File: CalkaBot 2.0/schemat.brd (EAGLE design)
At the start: 94.4 x 101.8 mm, 55 parts, among them IC1 TB6612FNG, IC2 LM339D, IC3 7806DT, Q1 16MHz, X1 MINI-USB-32005-301

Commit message: niezapisane rzeczt
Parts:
- added U$2, U$4, U$5: (no value), untitled:GND@1
- added U$3: (no value), untitled:GND
- moved X1 80.3 mm to (8.10, 81.7)
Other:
- board text added: "A1"
- board text added: "A2"
- board text added: "A4"
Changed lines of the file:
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@@
 <grid distance="0.1" unitdist="mm" unit="mm" style="lines" multiple="1" display="yes" altdistance="0.01" altunitdist="mm" altunit="mm"/>
 <layers>
-<layer number="1" name="Top" color="4" fill="1" visible="yes" active="yes"/>
+<layer number="1" name="Top" color="4" fill="1" visible="no" active="yes"/>
 <layer number="16" name="Bottom" color="1" fill="1" visible="yes" active="yes"/>
 <layer number="17" name="Pads" color="2" fill="1" visible="yes" active="yes"/>
 <layer number="18" name="Vias" color="2" fill="1" visible="yes" active="yes"/>
-<layer number="19" name="Unrouted" color="6" fill="1" visible="yes" active="yes"/>
-<layer number="20" name="Dimension" color="24" fill="1" visible="yes" active="yes"/>
-<layer number="21" name="tPlace" color="7" fill="1" visible="yes" active="yes"/>
-<layer number="22" name="bPlace" color="7" fill="1" visible="yes" active="yes"/>
-<layer number="23" name="tOrigins" color="15" fill="1" visible="yes" active="yes"/>
-<layer number="24" name="bOrigins" color="15" fill="1" visible="yes" active="yes"/>
-<layer number="25" name="tNames" color="7" fill="1" visible="yes" active="yes"/>
-<layer number="26" name="bNames" color="7" fill="1" visible="yes" active="yes"/>
-<layer number="27" name="tValues" color="7" fill="1" visible="yes" active="yes"/>
-<layer number="28" name="bValues" color="7" fill="1" visible="yes" active="yes"/>
+<layer number="19" name="Unrouted" color="6" fill="1" visible="no" active="yes"/>
+<layer number="20" name="Dimension" color="24" fill="1" visible="no" active="yes"/>
+<layer number="21" name="tPlace" color="7" fill="1" visible="no" active="yes"/>
+<layer number="22" name="bPlace" color="7" fill="1" visible="no" active="yes"/>
+<layer number="23" name="tOrigins" color="15" fill="1" visible="no" active="yes"/>
+<layer number="24" name="bOrigins" color="15" fill="1" visible="no" active="yes"/>
+<layer number="25" name="tNames" color="7" fill="1" visible="no" active="yes"/>
+<layer number="26" name="bNames" color="7" fill="1" visible="no" active="yes"/>
+<layer number="27" name="tValues" color="7" fill="1" visible="no" active="yes"/>
+<layer number="28" name="bValues" color="7" fill="1" visible="no" active="yes"/>
 <layer number="29" name="tStop" color="7" fill="3" visible="no" active="yes"/>
 <layer number="30" name="bStop" color="7" fill="6" visible="no" active="yes"/>
@@
 <layer number="37" name="tTest" color="7" fill="1" visible="no" active="yes"/>
 <layer number="38" name="bTest" color="7" fill="1" visible="no" active="yes"/>
-<layer number="39" name="tKeepout" color="4" fill="11" visible="yes" active="yes"/>
-<layer number="40" name="bKeepout" color="1" fill="11" visible="yes" active="yes"/>
-<layer number="41" name="tRestrict" color="4" fill="10" visible="yes" active="yes"/>
-<layer number="42" name="bRestrict" color="1" fill="10" visible="yes" active="yes"/>
+<layer number="39" name="tKeepout" color="4" fill="11" visible="no" active="yes"/>
+<layer number="40" name="bKeepout" color="1" fill="11" visible="no" active="yes"/>
+<layer number="41" name="tRestrict" color="4" fill="10" visible="no" active="yes"/>
+<layer number="42" name="bRestrict" color="1" fill="10" visible="no" active="yes"/>
 <layer number="43" name="vRestrict" color="2" fill="10" visible="no" active="yes"/>
-<layer number="44" name="Drills" color="7" fill="1" visible="yes" active="yes"/>
-<layer number="45" name="Holes" color="7" fill="1" visible="yes" active="yes"/>
+<layer number="44" name="Drills" color="7" fill="1" visible="no" active="yes"/>
+<layer number="45" name="Holes" color="7" fill="1" visible="no" active="yes"/>
 <layer number="46" name="Milling" color="3" fill="1" visible="no" active="yes"/>
 <layer number="47" name="Measures" color="7" fill="1" visible="no" active="yes"/>
@@
 <layer number="49" name="Reference" color="7" fill="1" visible="no" active="yes"/>
 <layer number="50" name="dxf" color="7" fill="1" visible="no" active="no"/>
-<layer number="51" name="tDocu" color="7" fill="1" visible="yes" active="yes"/>
-<layer number="52" name="bDocu" color="7" fill="1" visible="yes" active="yes"/>
+<layer number="51" name="tDocu" color="7" fill="1" visible="no" active="yes"/>
+<layer number="52" name="bDocu" color="7" fill="1" visible="no" active="yes"/>
 <layer number="53" name="tGND_GNDA" color="7" fill="9" visible="no" active="no"/>
 <layer number="54" name="bGND_GNDA" color="1" fill="9" visible="no" active="no"/>
@@
 <text x="17" y="8.7" size="1.016" layer="16" font="vector" ratio="25" rot="MR0" align="center">S4</text>
 <text x="83.2" y="8.6" size="1.016" layer="16" font="vector" ratio="25" rot="MR0" align="center">A3</text>
+<text x="14.7" y="66.2" size="1.016" layer="16" font="vector" ratio="25" rot="MR0" align="center">A2</text>
+<text x="14.7" y="8.7" size="1.016" layer="16" font="vector" ratio="25" rot="MR0" align="center">A4</text>
+<text x="83.1" y="66.2" size="1.016" layer="16" font="vector" ratio="25" rot="MR0" align="center">A1</text>
 </plain>
 <attributes>
@@
 <attribute name="OC_NEWARK" value="36M3542" x="24.2" y="3.8" size="1.778" layer="28" rot="MR0" display="off"/>
 </element>
-<element name="X1" library="con-cypressindustries" library_urn="urn:adsk.eagle:library:138" package="32005-301" package3d_urn="urn:adsk.eagle:package:6446/1" value="MINI-USB-32005-301" x="88.1" y="75.2" rot="MR270">
-<attribute name="MF" value="" x="88.1" y="75.2" size="1.778" layer="28" rot="MR270" display="off"/>
-<attribute name="MPN" value="" x="88.1" y="75.2" size="1.778" layer="28" rot="MR270" display="off"/>
-<attribute name="OC_FARNELL" value="unknown" x="88.1" y="75.2" size="1.778" layer="28" rot="MR270" display="off"/>
-<attribute name="OC_NEWARK" value="unknown" x="88.1" y="75.2" size="1.778" layer="28" rot="MR270" display="off"/>
+<element name="X1" library="con-cypressindustries" library_urn="urn:adsk.eagle:library:138" package="32005-301" package3d_urn="urn:adsk.eagle:package:6446/1" value="MINI-USB-32005-301" x="8.1" y="81.7" rot="MR270">
+<attribute name="MF" value="" x="8.1" y="81.7" size="1.778" layer="28" rot="MR270" display="off"/>
+<attribute name="MPN" value="" x="8.1" y="81.7" size="1.778" layer="28" rot="MR270" display="off"/>
+<attribute name="OC_FARNELL" value="unknown" x="8.1" y="81.7" size="1.778" layer="28" rot="MR270" display="off"/>
+<attribute name="OC_NEWARK" value="unknown" x="8.1" y="81.7" size="1.778" layer="28" rot="MR270" display="off"/>
 </element>
 <element name="R6" library="rcl" library_urn="urn:adsk.eagle:library:334" package="R0805" package3d_urn="urn:adsk.eagle:package:23553/2" value="10k" x="24.3" y="21.8" rot="R270">
@@
 <element name="JP2" library="pinhead" library_urn="urn:adsk.eagle:library:325" package="1X05" package3d_urn="urn:adsk.eagle:package:22469/2" value="" x="27.5" y="39.9" rot="MR90"/>
 <element name="JP3" library="pinhead" library_urn="urn:adsk.eagle:library:325" package="1X05" package3d_urn="urn:adsk.eagle:package:22469/2" value="" x="20.9" y="39.9" rot="MR90"/>
+<element name="U$2" library="untitled" package="GND@1" value="" x="85.5" y="8.5"/>
+<element name="U$4" library="untitled" package="GND@1" value="" x="85.4" y="66"/>
+<element name="U$5" library="untitled" package="GND@1" value="" x="12.4" y="66"/>
+<element name="U$3" library="untitled" package="GND" value="" x="-39.5" y="-20.7">
+<attribute name="UZ" value="gnd" x="-39.5" y="-20.7" size="1.778" layer="27" display="off"/>
+</element>
 </elements>
 <signals>
@@
 <wire x1="85.4" y1="59.33555" x2="85.4" y2="67.7" width="0.4" layer="1"/>
 <wire x1="84.2" y1="56" x2="85.48389375" y2="57.28389375" width="0.4" layer="1"/>
-<wire x1="85.48389375" y1="57.28389375" x2="85.48389375" y2="58.1" width="0.4" layer="1"/>
-<wire x1="85.48389375" y1="58.1" x2="85.48389375" y2="59.25165625" width="0.4" layer="1"/>
-<wire x1="87.3" y1="72.2" x2="86.5" y2="72.2" width="0" layer="19" extent="16-16"/>
-<wire x1="85.4" y1="67.7" x2="86.5" y2="72.2" width="0" layer="19" extent="16-16"/>
+<wire x1="85.48389375" y1="57.28389375" x2="85.48389375" y2="59.25165625" width="0.4" layer="1"/>
+<wire x1="7.3" y1="78.7" x2="6.5" y2="78.7" width="0" layer="19" extent="16-16"/>
+<wire x1="85.4" y1="67.7" x2="6.5" y2="78.7" width="0" layer="19" extent="16-16"/>
 <wire x1="20.9" y1="34.82" x2="20.9488" y2="32.3606" width="0" layer="19" extent="1-1"/>
 <wire x1="27.4512" y1="25.4606" x2="28.4" y2="30.1" width="0" layer="19" extent="1-1"/>
 <wire x1="27.4512" y1="18.5606" x2="20.9488" y2="18.5606" width="0" layer="19" extent="1-1"/>
-<wire x1="85.48389375" y1="58.1" x2="85.48389375" y2="58.1" width="0.4" layer="1"/>
 </signal>
 <signal name="RST">
@@
 <contactref element="JP3" pad="5"/>
 <wire x1="20.9" y1="44.98" x2="27.5" y2="44.98" width="0.4" layer="16"/>
-<wire x1="46.684465625" y1="33.78309375" x2="89.7" y2="72.2" width="0" layer="19" extent="1-16"/>
+<wire x1="46.684465625" y1="33.78309375" x2="9.7" y2="78.7" width="0" layer="19" extent="1-16"/>
 <wire x1="27.5" y1="44.98" x2="29.23005" y2="44.98" width="0" layer="19" extent="16-16"/>
 </signal>
@@
 <wire x1="20.9" y1="39.9" x2="27.5" y2="39.9" width="0.4" layer="16"/>
 <wire x1="27.5" y1="39.9" x2="27.6" y2="39.8" width="0.4" layer="16"/>
-<wire x1="33.3422875" y1="38.389946875" x2="88.1" y2="72.2" width="0" layer="19" extent="16-16"/>
+<wire x1="33.3422875" y1="38.389946875" x2="8.1" y2="78.7" width="0" layer="19" extent="16-16"/>
 </signal>
 <signal name="N$20">
@@
 <wire x1="31.26" y1="42.44" x2="27.5" y2="42.44" width="0.4" layer="16"/>
 <wire x1="27.5" y1="42.44" x2="20.9" y2="42.44" width="0.4" layer="16"/>
-<wire x1="35.4" y1="38.3" x2="88.9" y2="72.2" width="0" layer="19" extent="1-16"/>
+<wire x1="35.4" y1="38.3" x2="8.9" y2="78.7" width="0" layer="19" extent="1-16"/>
 </signal>
 <signal name="N$2">

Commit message: dodalem dipy
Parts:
- removed BUT1, BUT2, BUT3: (no value), switch-omron:B3F-10XX
- removed JP3: (no value), pinhead:1X05
- removed X1: MINI-USB-32005-301, con-cypressindustries:32005-301
- added SW2: (no value), special:EDG-03
- moved R2 8.16 mm to (25.3, 23.0), turned to 0 degrees
- moved R6 3.83 mm to (25.3, 25.5), turned to 0 degrees
- moved C10 2.94 mm to (34.8, 30.6)
- moved R9 1.17 mm to (25.3, 28.1), turned to 0 degrees
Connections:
- removed net N$20: JP2.4, JP3.4, R26.1, X1.4
- new net N$11: JP2.4, R26.1
- net GND: now also SW2.4, SW2.5, SW2.6; no longer BUT1.1, BUT1.2, BUT2.1, BUT2.2, BUT3.1, BUT3.2, JP3.1, JP3.2, X1.1, X1.2
- net MISO: now also SW2.3; no longer BUT1.3, BUT1.4
- net MOSI: now also SW2.2; no longer BUT2.3, BUT2.4
- net N$12: no longer JP3.3, X1.3
- net SCK: now also SW2.1; no longer BUT3.3, BUT3.4
- net VBUS: no longer JP3.5, X1.5
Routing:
- net VCC: track 297.7 -> 339.1 mm, vias 5 -> 4
- net N$20: track 18.0 -> 0.00 mm, vias 1 -> 0
- net MISO: track 35.7 -> 26.3 mm
- net MOSI: track 33.1 -> 25.8 mm
- net N$12: track 15.0 -> 8.41 mm
- net SCK: track 29.0 -> 23.5 mm
- net VBUS: track 36.9 -> 32.0 mm
- net GND: track 446.3 -> 441.9 mm, vias 5 -> 6
- net UCAP: track 14.6 -> 11.4 mm
- net VM: track 80.7 -> 80.1 mm

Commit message: połączono wszystkie VCC i GND
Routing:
- net VCC: track 339.1 -> 454.4 mm, vias 4 -> 5
- net N$11: track 0.00 -> 12.2 mm
- net GND: track 441.9 -> 450.5 mm
- net PIN: track 26.4 -> 25.2 mm
- net MOSI: track 25.8 -> 24.9 mm
- net N$12: vias 1 -> 0

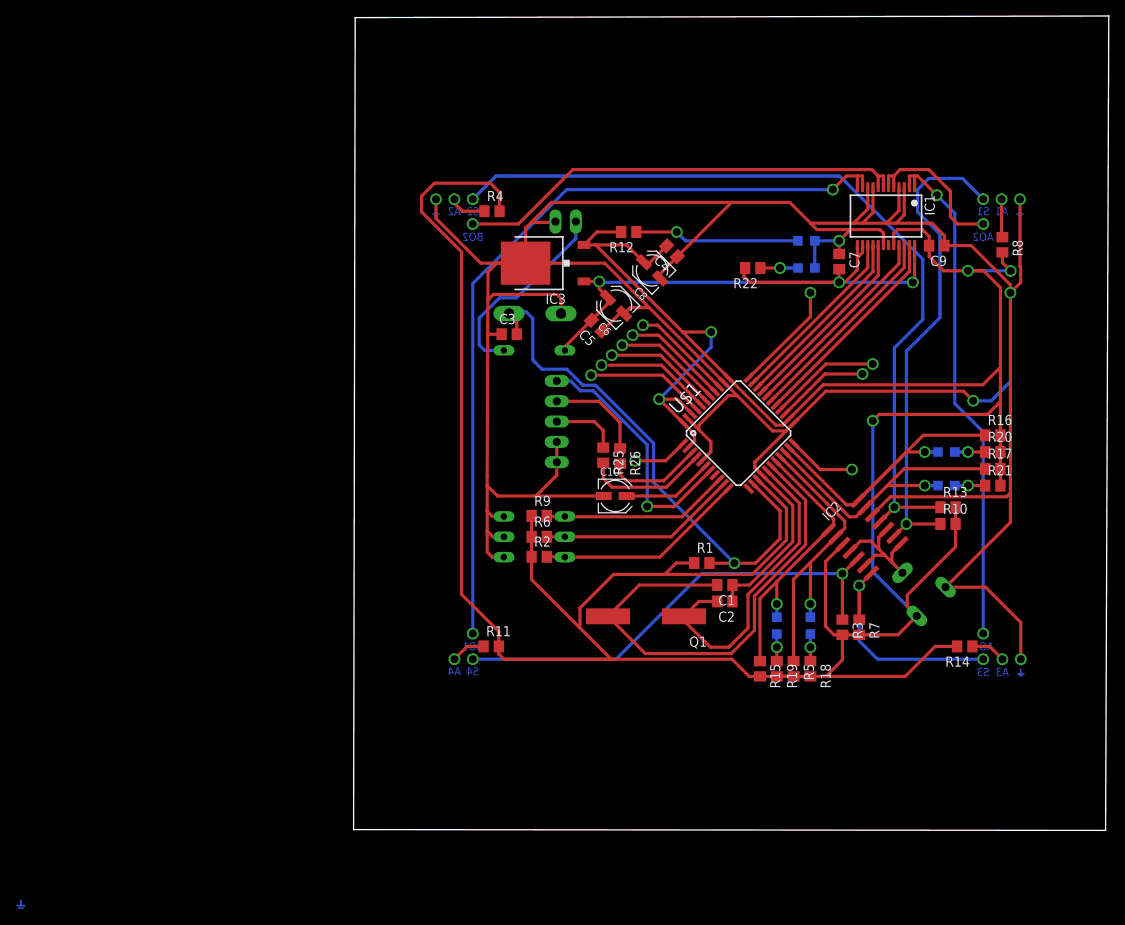
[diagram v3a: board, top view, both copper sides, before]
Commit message: dodano diode
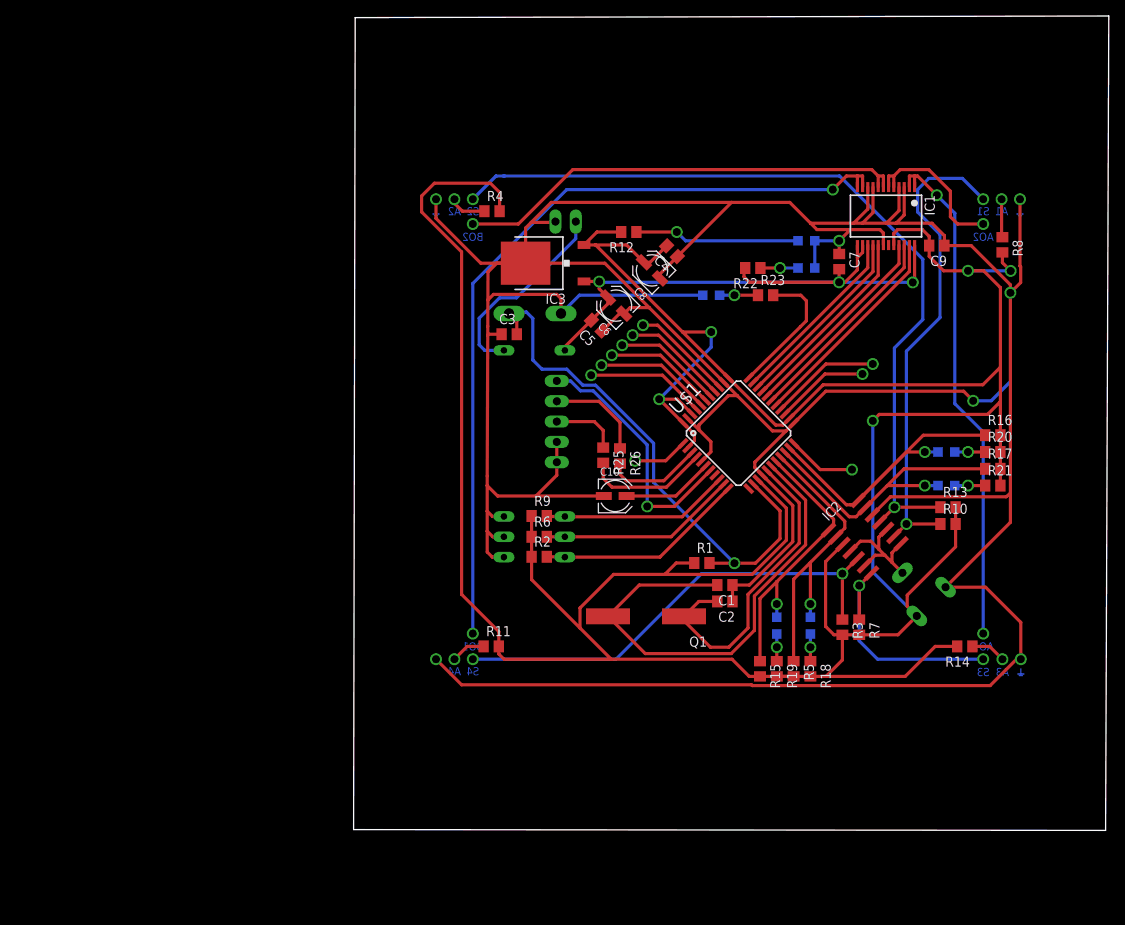
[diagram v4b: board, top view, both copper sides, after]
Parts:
- removed U$3: (no value), untitled:GND
- added LED7: (no value), led:CHIP-LED0805
- added R23: 220R, rcl:R0805
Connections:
- new net N$2: LED7.A, R23.1
- net GND: now also LED7.C
- net I/O10: now also R23.2
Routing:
- net GND: track 450.5 -> 545.0 mm, vias 6 -> 7
- net N$2: track 0.00 -> 4.80 mm, vias 0 -> 1
- net I/O10: track 13.8 -> 17.1 mm, vias 1 -> 0
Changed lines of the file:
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@@
 <text x="80.8" y="63" size="1.016" layer="16" font="vector" ratio="25" rot="MR0" align="center">AO2</text>
 <text x="80.8" y="11.8" size="1.016" layer="16" font="vector" ratio="25" rot="MR0" align="center">AO1</text>
-<wire x1="17" y1="85.1" x2="17.8" y2="85.9" width="0.4" layer="19"/>
 <text x="80.8" y="66.2" size="1.016" layer="16" font="vector" ratio="25" rot="MR0" align="center">S1</text>
 <text x="17" y="66.2" size="1.016" layer="16" font="vector" ratio="25" rot="MR0" align="center">S2</text>
@@
 <element name="U$4" library="untitled" package="GND@1" value="" x="85.4" y="66" smashed="yes"/>
 <element name="U$5" library="untitled" package="GND@1" value="" x="12.4" y="66" smashed="yes"/>
-<element name="U$3" library="untitled" package="GND" value="" x="-39.5" y="-20.7" smashed="yes">
-<attribute name="UZ" value="gnd" x="-39.5" y="-20.7" size="1.778" layer="27" display="off"/>
-</element>
 <element name="SW2" library="special" library_urn="urn:adsk.eagle:library:367" package="EDG-03" package3d_urn="urn:adsk.eagle:package:26663/2" value="" x="24.7" y="25.5" smashed="yes" rot="MR270">
 <attribute name="NAME" x="19.366" y="30.072" size="1.27" layer="26" ratio="10" rot="MR270"/>
 <attribute name="VALUE" x="31.304" y="30.072" size="1.27" layer="28" ratio="10" rot="MR270"/>
+</element>
+<element name="R23" library="rcl" library_urn="urn:adsk.eagle:library:334" package="R0805" package3d_urn="urn:adsk.eagle:package:23553/2" value="220R" x="53.6" y="55.7" smashed="yes">
+<attribute name="NAME" x="52.965" y="56.97" size="1.27" layer="25"/>
+<attribute name="SPICEPREFIX" value="R" x="53.6" y="55.7" size="1.778" layer="27" display="off"/>
+<attribute name="VALUE" x="52.965" y="53.16" size="1.27" layer="27"/>
+</element>
+<element name="LED7" library="led" library_urn="urn:adsk.eagle:library:259" package="CHIP-LED0805" package3d_urn="urn:adsk.eagle:package:15818/2" value="" x="46.8" y="55.7" smashed="yes" rot="MR270">
+<attribute name="NAME" x="48.07" y="56.97" size="1.27" layer="26" rot="MR0"/>
+<attribute name="VALUE" x="48.07" y="53.16" size="1.27" layer="28" rot="MR0"/>
 </element>
 </elements>
@@
 <contactref element="C9" pad="1"/>
 <contactref element="JP1" pad="1"/>
-<contactref element="LED5" pad="C"/>
 <wire x1="48.381521875" y1="44.813959375" x2="39.047740625" y2="54.147740625" width="0.4" layer="1"/>
 <wire x1="39.047740625" y1="54.147740625" x2="33.49548125" y2="59.7" width="0.4" layer="1"/>
@@
 <wire x1="40.407625" y1="57.792371875" x2="40.407625" y2="58.364121875" width="0.4" layer="1"/>
 <wire x1="40.407625" y1="58.364121875" x2="42.57175" y2="60.528246875" width="0.4" layer="1"/>
-<contactref element="LED6" pad="C"/>
 <wire x1="57.14964375" y1="39.722790625" x2="56.163425" y2="38.736571875" width="0.4" layer="1"/>
 <wire x1="67.025" y1="69.215" x2="67.025" y2="66.025" width="0.4" layer="1"/>
 <wire x1="67.025" y1="66.025" x2="65.7" y2="64.7" width="0.4" layer="1"/>
-<wire x1="59.75" y1="62.5" x2="59.75" y2="59.1" width="0.4" layer="16"/>
-<wire x1="59.75" y1="62.5" x2="62.8" y2="62.5" width="0.4" layer="16"/>
 <via x="62.8" y="62.5" extent="1-16" drill="1" diameter="1.3"/>
 <wire x1="62.8" y1="62.5" x2="64.2" y2="63.9" width="0.4" layer="1"/>
@@
 <wire x1="18.86901875" y1="50.699728125" x2="18.989290625" y2="50.82" width="0.4" layer="1"/>
 <wire x1="18.989290625" y1="50.82" x2="20.6" y2="50.82" width="0.4" layer="1"/>
+<contactref element="LED5" pad="C"/>
+<contactref element="LED6" pad="C"/>
+<wire x1="59.75" y1="62.5" x2="59.75" y2="59.1" width="0.4" layer="16"/>
+<wire x1="59.75" y1="62.5" x2="62.8" y2="62.5" width="0.4" layer="16"/>
+<contactref element="LED7" pad="C"/>
+<wire x1="45.75" y1="55.7" x2="30.321571875" y2="55.7" width="0.4" layer="16"/>
+<wire x1="30.321571875" y1="55.7" x2="28.02868125" y2="53.407109375" width="0.4" layer="16"/>
+<wire x1="85.5" y1="10.2" x2="84.96776875" y2="10.2" width="0.4" layer="1"/>
+<wire x1="51.94289375" y1="6.9" x2="51.84289375" y2="7" width="0.4" layer="1"/>
+<wire x1="84.96776875" y1="10.2" x2="81.66776875" y2="6.9" width="0.4" layer="1"/>
+<wire x1="81.66776875" y1="6.9" x2="51.94289375" y2="6.9" width="0.4" layer="1"/>
+<wire x1="15.6" y1="7" x2="12.4" y2="10.2" width="0.4" layer="1"/>
+<via x="12.4" y="10.2" extent="1-16" drill="1" diameter="1.3"/>
+<wire x1="51.84289375" y1="7" x2="15.6" y2="7" width="0.4" layer="1"/>
 </signal>
 <signal name="RST">
@@
 <signal name="I/O10">
 <contactref element="U$1" pad="33"/>
-<wire x1="51.492790625" y1="45.37964375" x2="59.2" y2="52.986853125" width="0.4" layer="1"/>
-<via x="59.2" y="56" extent="1-16" drill="1" diameter="1.3"/>
-<wire x1="59.2" y1="52.986853125" x2="59.2" y2="56" width="0.4" layer="1"/>
+<wire x1="51.492790625" y1="45.37964375" x2="57.94879375" y2="51.75188125" width="0.4" layer="1"/>
+<wire x1="58.7" y1="55" x2="58" y2="55.7" width="0.4" layer="1"/>
+<wire x1="57.94879375" y1="51.75188125" x2="58.7" y2="52.5030875" width="0.4" layer="1"/>
+<wire x1="58.7" y1="52.5030875" x2="58.7" y2="55" width="0.4" layer="1"/>
+<contactref element="R23" pad="2"/>
+<wire x1="54.55" y1="55.7" x2="58" y2="55.7" width="0.4" layer="1"/>
 </signal>
 <signal name="PIN">
@@
 <wire x1="35.4" y1="39.8" x2="32.76" y2="42.44" width="0.4" layer="1"/>
 </signal>
+<signal name="N$2">
+<contactref element="R23" pad="1"/>
+<contactref element="LED7" pad="A"/>
+<wire x1="52.65" y1="55.7" x2="49.7" y2="55.7" width="0.4" layer="1"/>
+<via x="49.7" y="55.7" extent="1-16" drill="1" diameter="1.3"/>
+<wire x1="49.7" y1="55.7" x2="47.85" y2="55.7" width="0.4" layer="16"/>
+</signal>
 </signals>

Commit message: chyba skończyłem
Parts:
- added U$3: (no value), untitled:GND@1
- moved U$5 5.41 mm to (12.7, 71.4)
- moved U$2 1.73 mm to (85.8, 10.2)
- moved R14 1.53 mm to (78.8, 10.3)
- moved LED1 0.70 mm to (59.2, 15.1)
- moved LED2 0.70 mm to (55.0, 15.1)
- moved R15 0.70 mm to (52.9, 9.70)
- moved R18 0.70 mm to (59.2, 9.70)
- moved R19 0.70 mm to (55.0, 9.70)
- moved R5 0.70 mm to (57.1, 9.70)
- moved U$4 0.10 mm to (85.4, 66.1)
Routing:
- net GND: track 545.0 -> 481.3 mm
- net BO1: track 100.8 -> 57.1 mm
- net VCC: track 454.4 -> 432.6 mm, vias 5 -> 7
- net N$1: track 4.66 -> 8.38 mm
- net AO1: track 64.4 -> 66.0 mm, vias 2 -> 3
- net FL1: track 38.5 -> 37.1 mm
- net FL2: track 36.2 -> 34.8 mm
- net S2: track 29.8 -> 30.7 mm
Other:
- board size 94.4 x 101.8 mm -> 94.2 x 84.6 mm
